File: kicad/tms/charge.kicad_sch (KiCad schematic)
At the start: 33 parts, among them K1 AZ9861-1C-24DC2R1, Q1 NPN, T1 Transformer_1P_1S, U1 VO2611, U2 VO2611, U7 LM393

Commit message: Kicad files
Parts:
- added BT: 9V, symbol Device:Battery
- added C10: C, symbol Device:C
- added R1: 1kΩ, symbol Device:R
- added R2, R3: 5.6kΩ, symbol Device:R
- added U7: IL300, symbol Isolator_Analog:IL300
- added U8, U9: UA741, Package_TO_SOT_SMD:SOT-23-5, symbol Amplifier_Operational:ADA4610-1xRJ
- renumbered D28 to D10, D36 to D11, D35 to D12, D34 to D13, D33 to D14, D32 to D15, D31 to D16, D30 to D17, D29 to D18, D1 to D2, D21 to D3, D22 to D4, D23 to D5, D24 to D6, D25 to D7, D26 to D8, D27 to D9, Q1 to Q2, R1 to R11, R3 to R12, R4 to R13, R5 to R14, R6 to R15, U7 to U3
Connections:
- net Cap-: now also U2.2 (K), BT.2 (-), R2.2, U7.1, U8.2 (V-)
- net Divider: now also U8.3 (+)
- net GND: now also U9.2 (V-), U9.3 (+); no longer U2.2 (K)
- new net: R1.2, U7.2
- new net: BT.1 (+), U7.3, U8.5 (V+)
- new net: C10.2, R2.1, U7.4, U8.4 (-)
- new net: R3.1, U7.5, U9.4 (-)
- new net: C10.1, R1.1, U8.1
- new net CAP VOLTAGE: R3.2, U9.1
- new net PSU 12V: U7.6, U9.5 (V+)
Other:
- note added: "Comparator Circuit"
- note added: "Linear Optocoupler Circuit"
- moved on the sheet: D10, D2, D3, D4, D5, D6, D7, D8, D9, F1, K1, Q2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

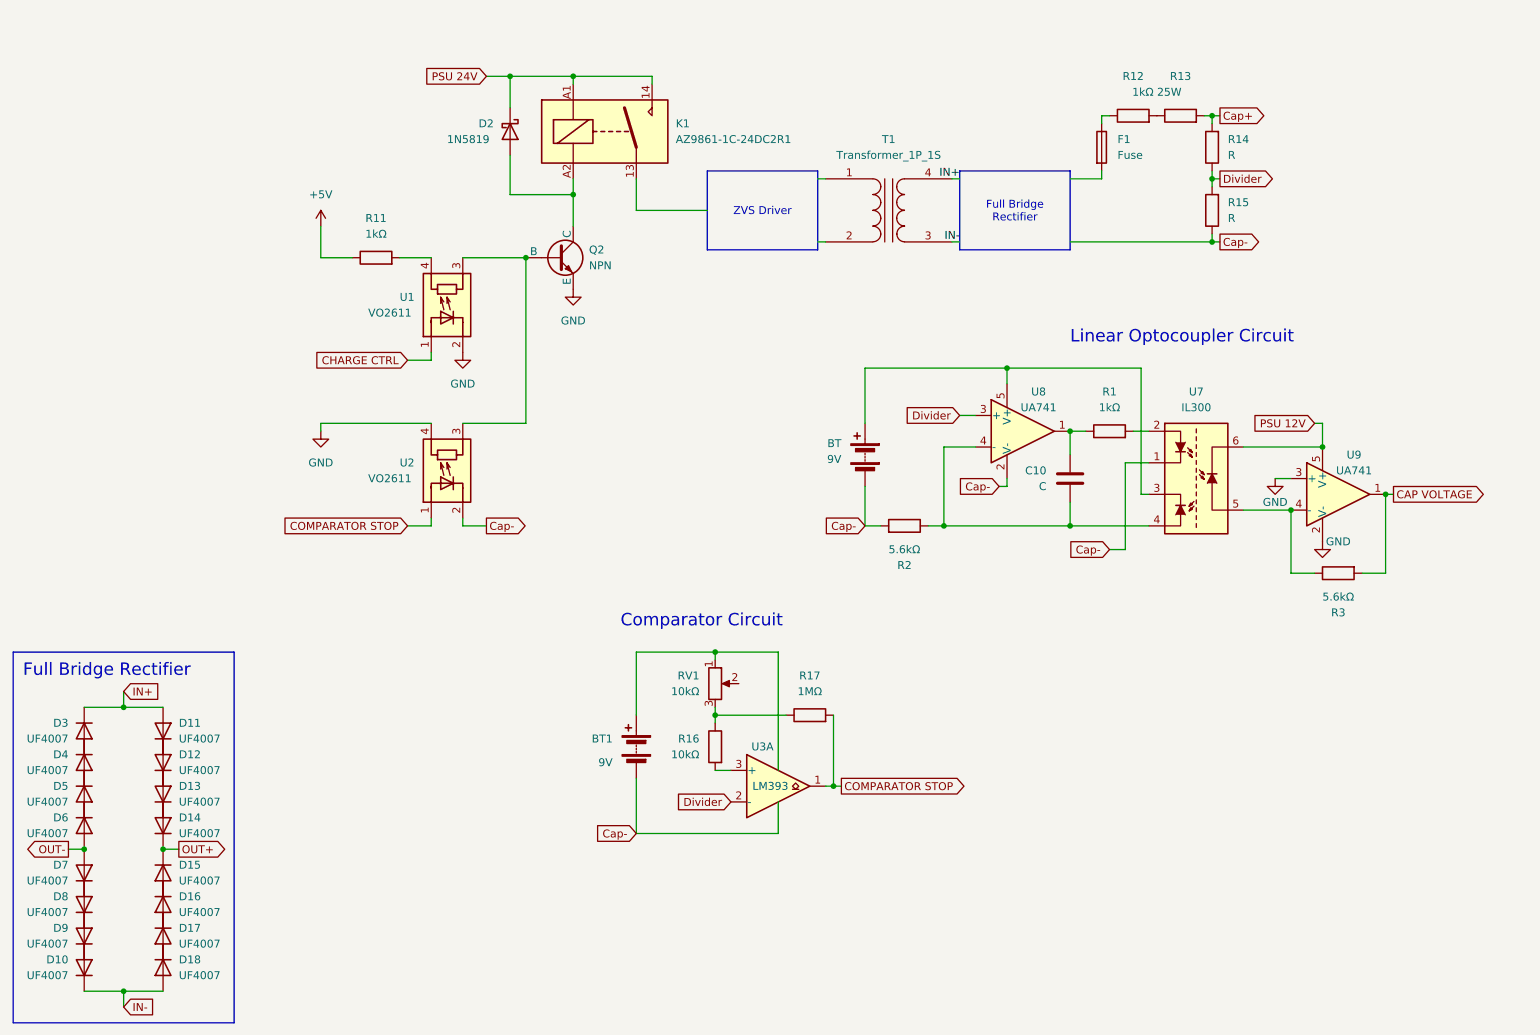
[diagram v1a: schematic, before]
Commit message: Schematic fixes after real life tests
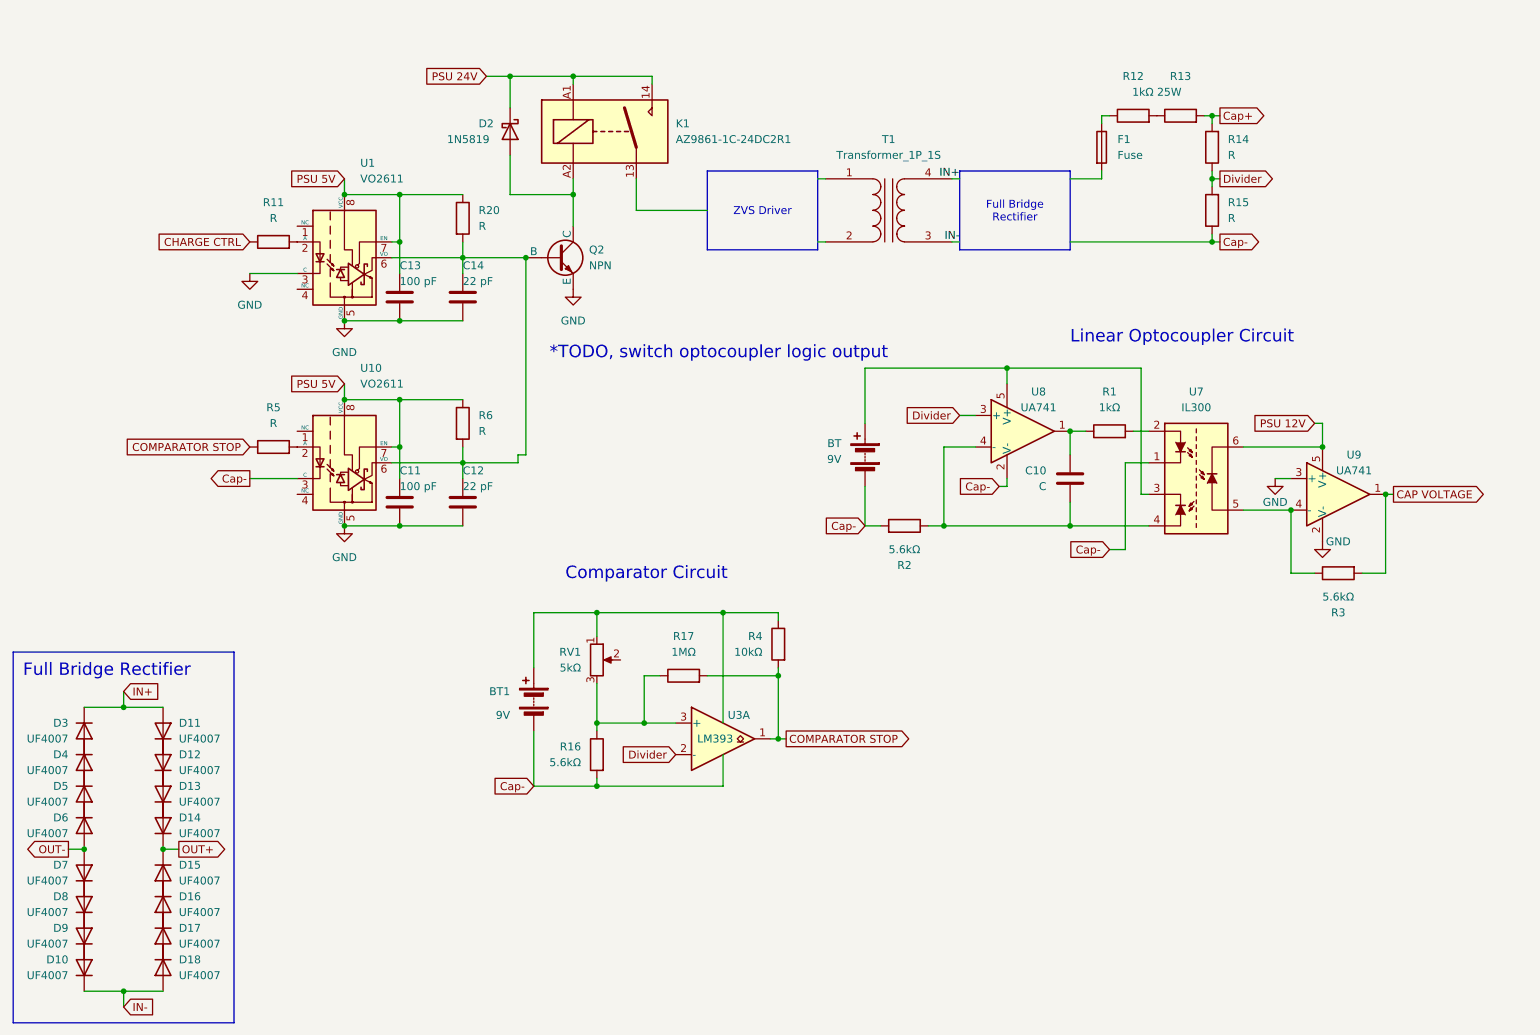
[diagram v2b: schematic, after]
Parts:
- removed U1, U2: VO2611, OptoDevice:Luna_NSL-32, symbol Isolator:NSL-32
- added C11, C13: 100 pF, symbol Device:C
- added C12, C14: 22 pF, symbol Device:C
- added R20, R5, R6: R, symbol Device:R
- added R4: 10kΩ, symbol Device:R
- added U1, U10: VO2611, Package_DIP:DIP-8_W7.62mm, symbol Isolator:VO2611
- R11: value 1kΩ -> R
- R16: value 10kΩ -> 5.6kΩ
- RV1: value 10kΩ -> 5kΩ
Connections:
- net +5V is gone; now on net CHARGE CTRL: R11.1
- net COMPARATOR STOP: now also R4.2, R5.1
- net Cap-: now also R16.2, U10.3 (C)
- net GND: now also C11.2, C12.2, C13.2, C14.2, U1.3 (C), U1.5 (GND), U10.5 (GND)
- net at R11.2: now also U1.2 (A)
- net at BT1.1 (+), RV1.1: now also R4.1
- net at R16.1, R17.1, RV1.3: now also U3.3 (+)
- net at Q2.2 (B): now also C12.1, C14.1, R20.2, R6.2, U1.6 (VO), U10.6 (VO)
- new net: R5.2, U10.2 (A)
- new net PSU 5V: C11.1, C13.1, R20.1, R6.1, U1.7 (EN), U1.8 (VCC), U10.7 (EN), U10.8 (VCC)
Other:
- note added: "*TODO, switch optocoupler logic output"
- moved on the sheet: BT1, R16, R17, RV1, U3A

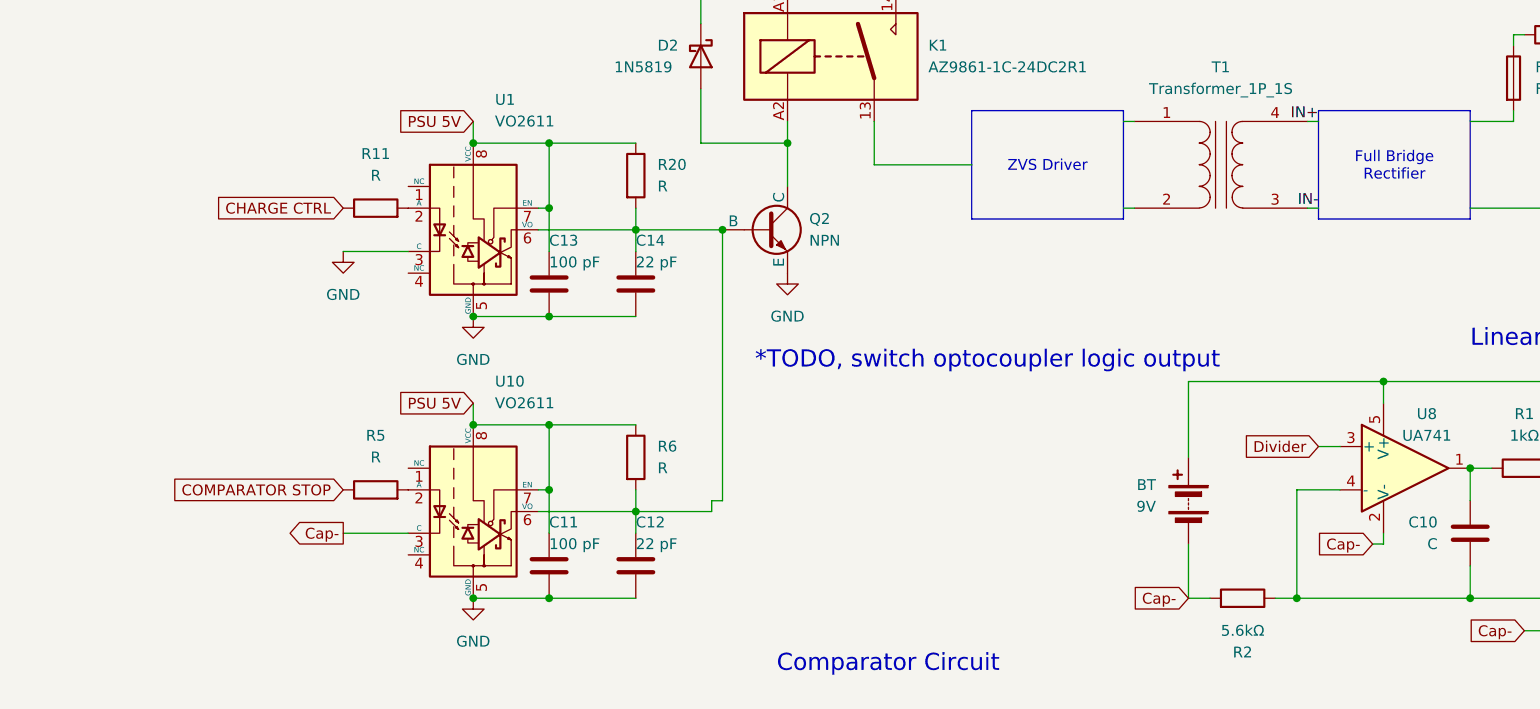
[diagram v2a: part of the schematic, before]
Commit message: Fixed optocoupler output logic
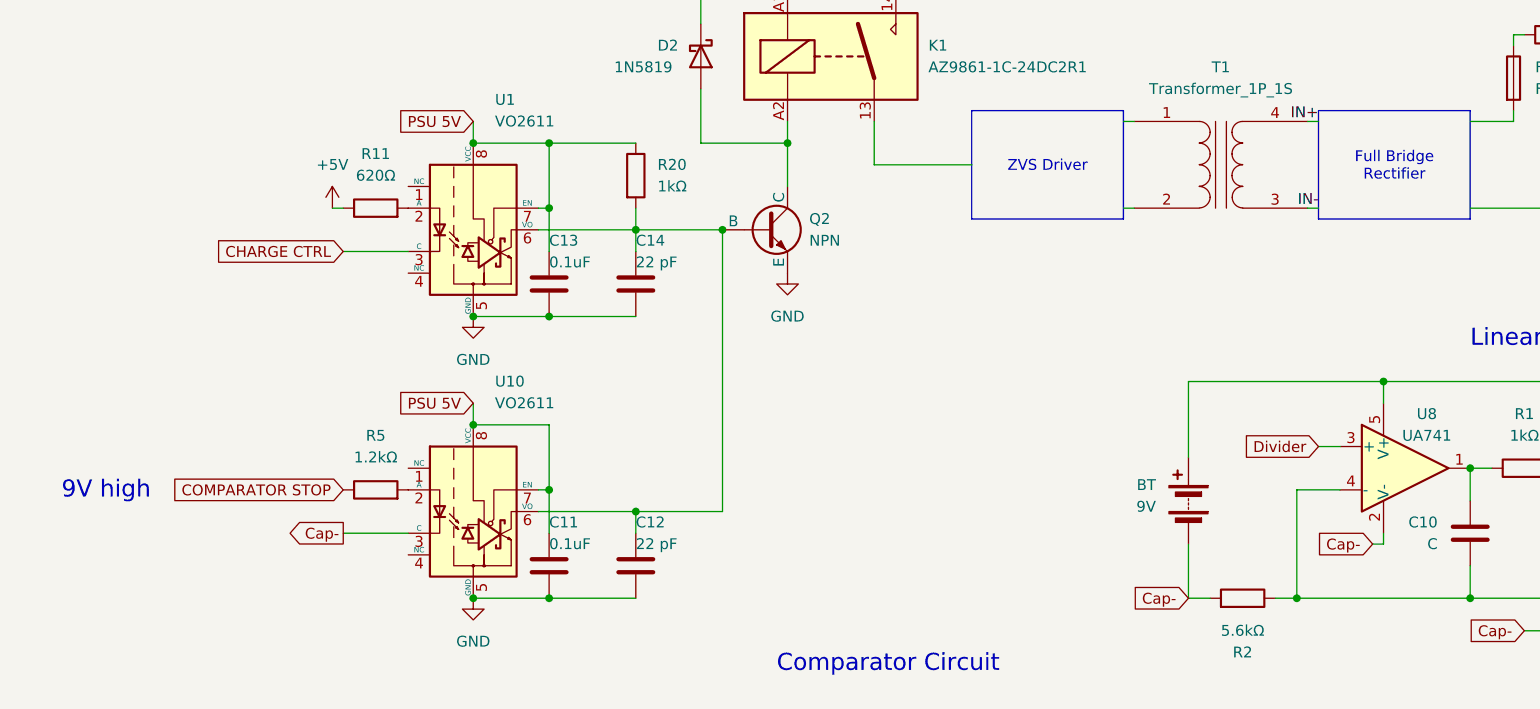
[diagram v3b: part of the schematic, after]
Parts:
- removed R6: R, symbol Device:R
- C11, C13: value 100 pF -> 0.1uF
- R11: value R -> 620Ω
- R20: value R -> 1kΩ
- R5: value R -> 1.2kΩ
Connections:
- net CHARGE CTRL: now also U1.3 (C); no longer R11.1
- net GND: no longer U1.3 (C)
- new net +5V: R11.1
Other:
- note added: "9V high"
- note removed: "*TODO, switch optocoupler logic output"
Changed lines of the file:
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@@
   (junction (at 73.66 91.44) (diameter 0) (color 0 0 0 0)
   )
-  (junction (at 82.55 91.44) (diameter 0) (color 0 0 0 0)
-  )
   (junction (at 114.3 143.51) (diameter 0) (color 0 0 0 0)
   )
@@
     (stroke (width 0) (type default))
   )
-  (wire (pts (xy 101.6 101.6) (xy 92.71 101.6))
+  (wire (pts (xy 92.71 101.6) (xy 102.87 101.6))
     (stroke (width 0) (type default))
   )
@@
     (stroke (width 0) (type default))
   )
-  (wire (pts (xy 101.6 100.33) (xy 101.6 101.6))
-    (stroke (width 0) (type default))
-  )
   (wire (pts (xy 110.49 39.37) (xy 110.49 40.64))
     (stroke (width 0) (type default))
@@
     (stroke (width 0) (type default))
   )
-  (wire (pts (xy 101.6 100.33) (xy 102.87 100.33))
-    (stroke (width 0) (type default))
-  )
   (wire (pts (xy 123.19 39.37) (xy 123.19 40.64))
     (stroke (width 0) (type default))
@@
     (stroke (width 0) (type default))
   )
-  (wire (pts (xy 82.55 91.44) (xy 92.71 91.44))
-    (stroke (width 0) (type default))
-  )
   (wire (pts (xy 96.52 39.37) (xy 100.33 39.37))
     (stroke (width 0) (type default))
@@
     (stroke (width 0) (type default))
   )
-  (wire (pts (xy 102.87 100.33) (xy 102.87 68.58))
-    (stroke (width 0) (type default))
-  )
   (wire (pts (xy 213.36 45.72) (xy 214.63 45.72))
     (stroke (width 0) (type default))
@@
     (stroke (width 0) (type default))
   )
-  (wire (pts (xy 92.71 99.06) (xy 92.71 101.6))
-    (stroke (width 0) (type default))
-  )
   (wire (pts (xy 38.1 138.43) (xy 38.1 140.97))
     (stroke (width 0) (type default))
@@
     (stroke (width 0) (type default))
   )
+  (wire (pts (xy 57.15 66.04) (xy 58.42 66.04))
+    (stroke (width 0) (type default))
+  )
   (wire (pts (xy 171.45 55.88) (xy 172.72 55.88))
     (stroke (width 0) (type default))
@@
   )
   (wire (pts (xy 114.3 137.16) (xy 114.3 143.51))
+    (stroke (width 0) (type default))
+  )
+  (wire (pts (xy 102.87 68.58) (xy 102.87 101.6))
     (stroke (width 0) (type default))
   )
@@
     (effects (font (size 2 2)) (justify left top))
   )
-  (text "*TODO, switch optocoupler logic output\n" (at 106.68 85.09 0)
-    (effects (font (size 2 2)) (justify left bottom))
-  )
   (text "Comparator Circuit" (at 109.22 120.65 0)
     (effects (font (size 2 2)) (justify left bottom))
   )
   (text "Linear Optocoupler Circuit" (at 190.5 82.55 0)
+    (effects (font (size 2 2)) (justify left bottom))
+  )
+  (text "9V high\n" (at 25.4 100.33 0)
     (effects (font (size 2 2)) (justify left bottom))
   )
@@
     )
   )
-  (global_label "CHARGE CTRL" (shape input) (at 58.42 66.04 180) (fields_autoplaced)
-    (effects (font (size 1.27 1.27)) (justify right))
-    (property "Intersheetrefs" "${INTERSHEET_REFS}" (at 42.5534 66.04 0)
-      (effects (font (size 1.27 1.27)) (justify right) hide)
-    )
-  )
   (global_label "Cap-" (shape input) (at 196.85 115.57 180) (fields_autoplaced)
     (effects (font (size 1.27 1.27)) (justify right))
@@
     )
   )
+  (global_label "CHARGE CTRL" (shape input) (at 58.42 71.12 180) (fields_autoplaced)
+    (effects (font (size 1.27 1.27)) (justify right))
+    (property "Intersheetrefs" "${INTERSHEET_REFS}" (at 42.5534 71.12 0)
+      (effects (font (size 1.27 1.27)) (justify right) hide)
+    )
+  )
   (global_label "PSU 12V" (shape input) (at 229.87 95.25 180) (fields_autoplaced)
     (effects (font (size 1.27 1.27)) (justify right))
@@
     )
   )
-  (symbol (lib_id "Device:R") (at 92.71 95.25 0) (unit 1)
-    (in_bom yes) (on_board yes) (dnp no) (fields_autoplaced)
-    (property "Reference" "R6" (at 95.25 93.98 0)
-      (effects (font (size 1.27 1.27)) (justify left))
-    )
-    (property "Value" "R" (at 95.25 96.52 0)
-      (effects (font (size 1.27 1.27)) (justify left))
-    )
-    (property "Footprint" "" (at 90.932 95.25 90)
-      (effects (font (size 1.27 1.27)) hide)
-    )
-    (property "Datasheet" "~" (at 92.71 95.25 0)
-      (effects (font (size 1.27 1.27)) hide)
-    )
-    (pin "1")
-    (pin "2")
-    (instances
-      (project "tms"
-        (path "/dc88686f-c772-4c63-b1cc-83a281c6b46c/52808854-7c95-4ac8-9e37-1a1e5d6f75e2"
-          (reference "R6") (unit 1)
-        )
-      )
-    )
-  )
   (symbol (lib_id "Device:D") (at 44.45 167.64 90) (mirror x) (unit 1)
     (in_bom yes) (on_board yes) (dnp no) (fields_autoplaced)
@@
         (path "/dc88686f-c772-4c63-b1cc-83a281c6b46c/52808854-7c95-4ac8-9e37-1a1e5d6f75e2"
           (reference "BT1") (unit 1)
-        )
-      )
-    )
-  )
-  (symbol (lib_id "power:GND") (at 58.42 71.12 0) (unit 1)
-    (in_bom yes) (on_board yes) (dnp no) (fields_autoplaced)
-    (property "Reference" "#PWR04" (at 58.42 77.47 0)
-      (effects (font (size 1.27 1.27)) hide)
-    )
-    (property "Value" "GND" (at 58.42 76.2 0)
-      (effects (font (size 1.27 1.27)))
-    )
-    (property "Footprint" "" (at 58.42 71.12 0)
-      (effects (font (size 1.27 1.27)) hide)
-    )
-    (property "Datasheet" "" (at 58.42 71.12 0)
-      (effects (font (size 1.27 1.27)) hide)
-    )
-    (pin "1")
-    (instances
-      (project "tms"
-        (path "/dc88686f-c772-4c63-b1cc-83a281c6b46c/52808854-7c95-4ac8-9e37-1a1e5d6f75e2"
-          (reference "#PWR04") (unit 1)
         )
       )
@@
       (effects (font (size 1.27 1.27)) (justify left))
     )
-    (property "Value" "100 pF" (at 82.55 72.39 0)
+    (property "Value" "0.1uF" (at 82.55 72.39 0)
       (effects (font (size 1.27 1.27)) (justify left))
     )
@@
       (effects (font (size 1.27 1.27)))
     )
-    (property "Value" "R" (at 62.23 95.25 90)
+    (property "Value" "1.2kΩ" (at 62.23 95.25 90)
       (effects (font (size 1.27 1.27)))
     )
@@
       (effects (font (size 1.27 1.27)) (justify left))
     )
-    (property "Value" "100 pF" (at 82.55 105.41 0)
+    (property "Value" "0.1uF" (at 82.55 105.41 0)
       (effects (font (size 1.27 1.27)) (justify left))
     )
@@
       (effects (font (size 1.27 1.27)) (justify left))
     )
-    (property "Value" "R" (at 95.25 63.5 0)
+    (property "Value" "1kΩ" (at 95.25 63.5 0)
       (effects (font (size 1.27 1.27)) (justify left))
     )
@@
       (effects (font (size 1.27 1.27)))
     )
-    (property "Value" "R" (at 62.23 62.23 90)
+    (property "Value" "620Ω" (at 62.23 62.23 90)
       (effects (font (size 1.27 1.27)))
     )
@@
         )
       )
+    )
+  )
+  (symbol (lib_id "power:+5V") (at 57.15 66.04 0) (unit 1)
+    (in_bom yes) (on_board yes) (dnp no) (fields_autoplaced)
+    (property "Reference" "#PWR04" (at 57.15 69.85 0)
+      (effects (font (size 1.27 1.27)) hide)
+    )
+    (property "Value" "+5V" (at 57.15 60.96 0)
+      (effects (font (size 1.27 1.27)))
+    )
+    (property "Footprint" "" (at 57.15 66.04 0)
+      (effects (font (size 1.27 1.27)) hide)
+    )
+    (property "Datasheet" "" (at 57.15 66.04 0)
+      (effects (font (size 1.27 1.27)) hide)
+    )
+    (pin "1")
+    (instances
+      (project "tms"
+        (path "/dc88686f-c772-4c63-b1cc-83a281c6b46c/52808854-7c95-4ac8-9e37-1a1e5d6f75e2"
+          (reference "#PWR04") (unit 1)
+        )
+      )
